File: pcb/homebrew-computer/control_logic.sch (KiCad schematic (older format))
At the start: 14 parts

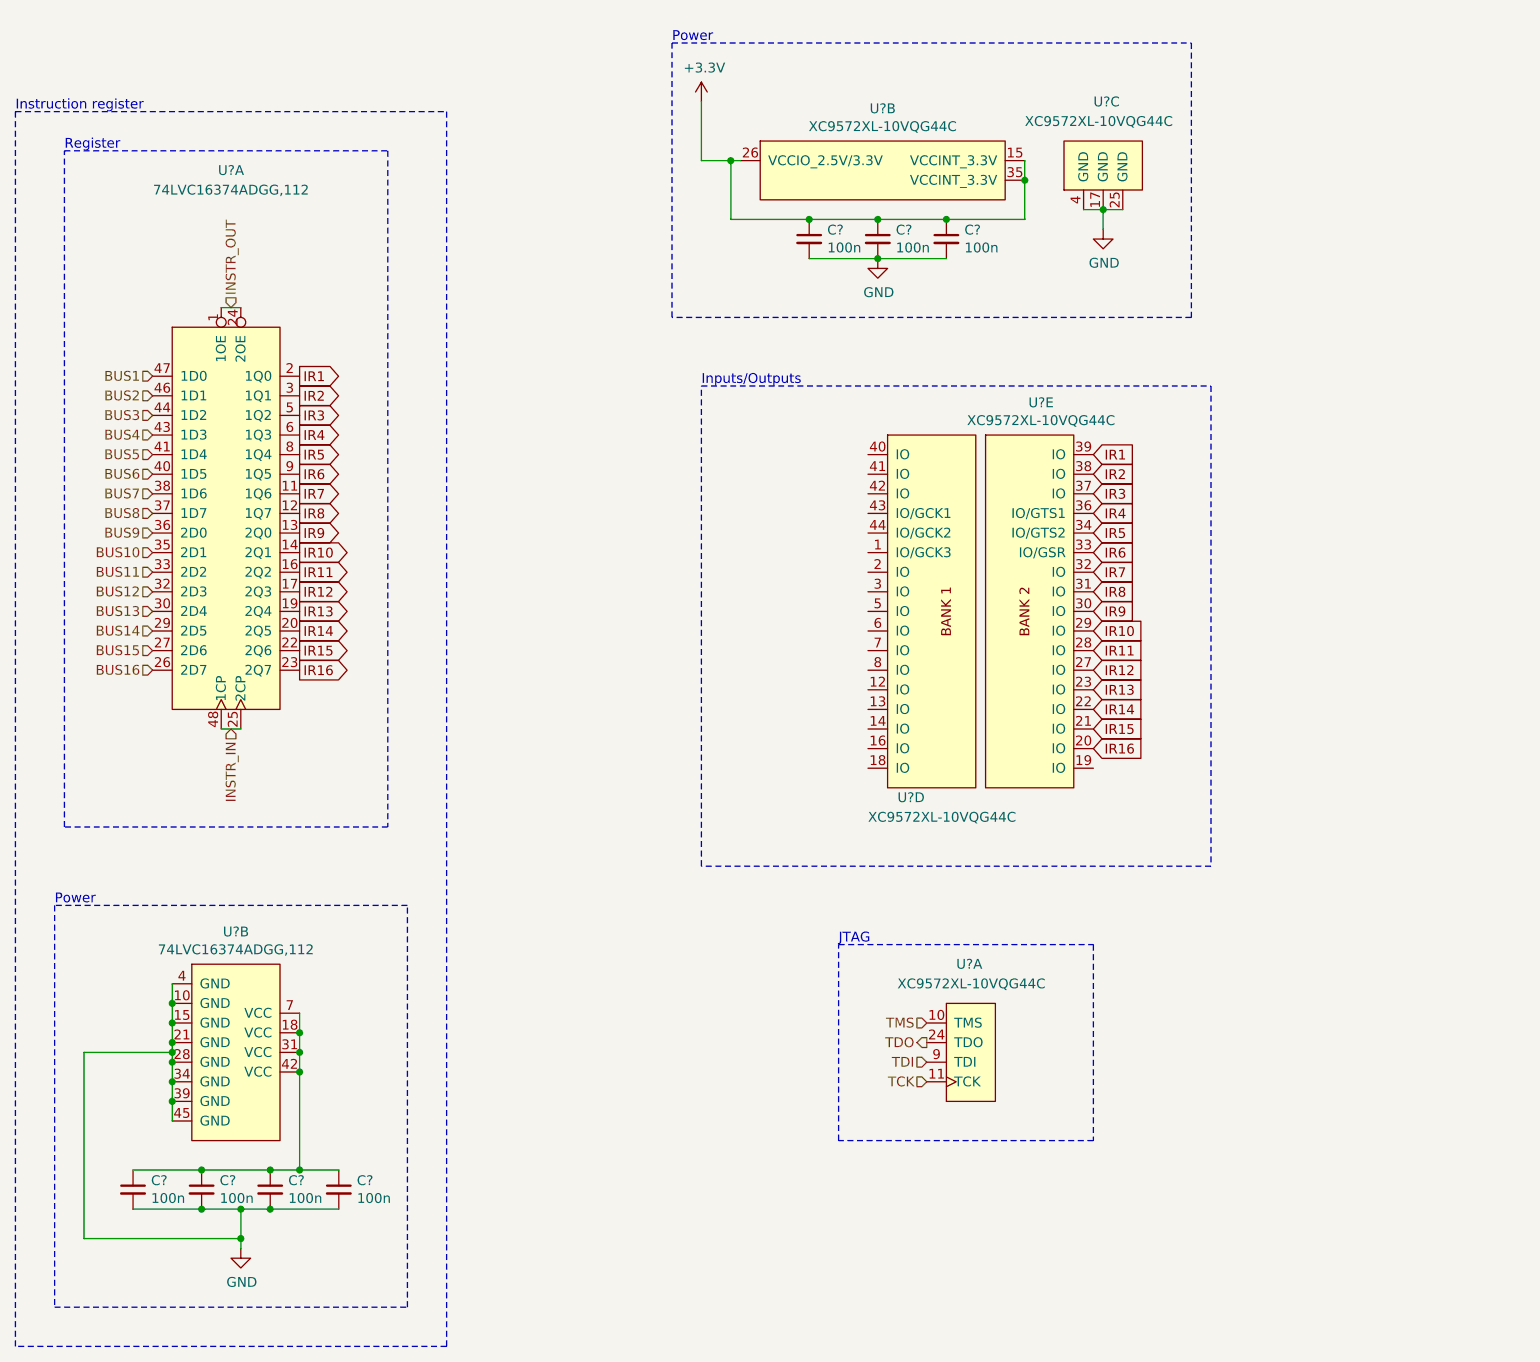
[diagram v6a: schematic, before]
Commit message: Change the control logic CPLD for a bigger one
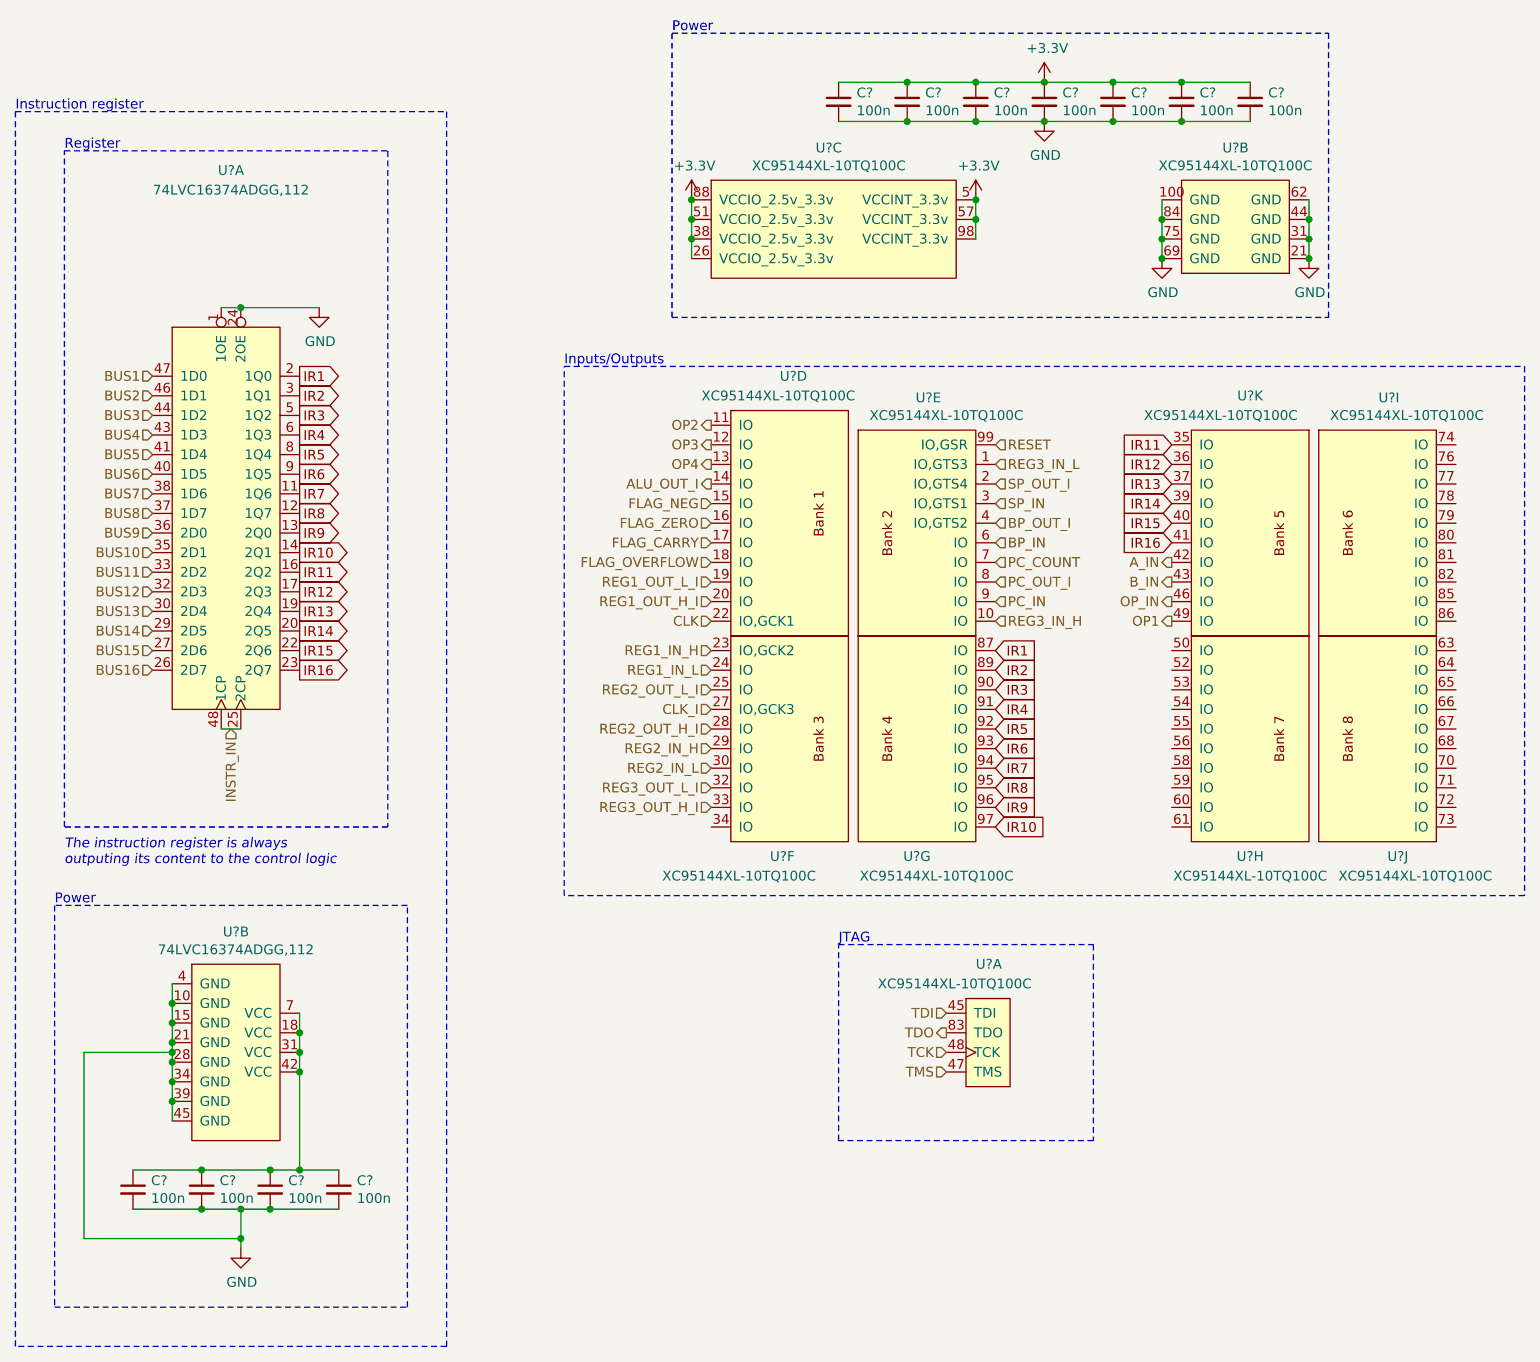
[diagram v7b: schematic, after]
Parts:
- removed U? (x5): XC9572XL-10VQG44C, symbol XC9500XL:XC9572XL-10VQG44C
- added C? (x4): 100n, symbol Device:C_Small
- added U? (x11): XC95144XL-10TQ100C, symbol XC9500XL:XC95144XL-10TQ100C
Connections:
- net INSTR_OUT is gone; now on net GND: U?.1 (1OE), U?.24 (2OE)
- net +3V3: now also C?.1, C?.1, C?.1, C?.1, U?.26 (VCCIO_2.5v_3.3v), U?.38 (VCCIO_2.5v_3.3v), U?.5 (VCCINT_3.3v), U?.51 (VCCIO_2.5v_3.3v), U?.57 (VCCINT_3.3v), U?.88 (VCCIO_2.5v_3.3v), U?.98 (VCCINT_3.3v)
- net GND: now also C?.2, C?.2, C?.2, C?.2, U?.100 (GND), U?.21 (GND), U?.31 (GND), U?.44 (GND), U?.62 (GND), U?.69 (GND), U?.75 (GND), U?.84 (GND)
- net IR1: now also U?.87 (IO)
- net IR10: now also U?.97 (IO)
- net IR11: now also U?.35 (IO)
- net IR12: now also U?.36 (IO)
- net IR13: now also U?.37 (IO)
- net IR14: now also U?.39 (IO)
- net IR15: now also U?.40 (IO)
- net IR16: now also U?.41 (IO)
- net IR2: now also U?.89 (IO)
- net IR3: now also U?.90 (IO)
- net IR4: now also U?.91 (IO)
- net IR5: now also U?.92 (IO)
- net IR6: now also U?.93 (IO)
- net IR7: now also U?.94 (IO)
- net IR8: now also U?.95 (IO)
- net IR9: now also U?.96 (IO)
- net TCK: now also U?.48 (TCK)
- net TDI: now also U?.45 (TDI)
- net TDO: now also U?.83 (TDO)
- net TMS: now also U?.47 (TMS)
- new net ALU_OUT_I: U?.14 (IO)
- new net A_IN: U?.42 (IO)
- new net BP_IN: U?.6 (IO)
- new net BP_OUT_I: U?.4 (IO,GTS2)
- new net B_IN: U?.43 (IO)
- new net CLK: U?.22 (IO,GCK1)
- new net CLK_I: U?.27 (IO,GCK3)
- new net FLAG_CARRY: U?.17 (IO)
- new net FLAG_NEG: U?.15 (IO)
- new net FLAG_OVERFLOW: U?.18 (IO)
- new net FLAG_ZERO: U?.16 (IO)
- new net OP1: U?.49 (IO)
- new net OP2: U?.11 (IO)
- new net OP3: U?.12 (IO)
- new net OP4: U?.13 (IO)
- new net OP_IN: U?.46 (IO)
- new net PC_COUNT: U?.7 (IO)
- new net PC_IN: U?.9 (IO)
- new net PC_OUT_I: U?.8 (IO)
- new net REG1_IN_H: U?.23 (IO,GCK2)
- new net REG1_IN_L: U?.24 (IO)
- new net REG1_OUT_H_I: U?.20 (IO)
- new net REG1_OUT_L_I: U?.19 (IO)
- new net REG2_IN_H: U?.29 (IO)
- new net REG2_IN_L: U?.30 (IO)
- new net REG2_OUT_H_I: U?.28 (IO)
- new net REG2_OUT_L_I: U?.25 (IO)
- new net REG3_IN_H: U?.10 (IO)
- new net REG3_IN_L: U?.1 (IO,GTS3)
- new net REG3_OUT_H_I: U?.33 (IO)
- new net REG3_OUT_L_I: U?.32 (IO)
- new net RESET: U?.99 (IO,GSR)
- new net SP_IN: U?.3 (IO,GTS1)
- new net SP_OUT_I: U?.2 (IO,GTS4)
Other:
- note added: "The instruction register is always\noutputing its content to the control logic"
- moved on the sheet: C?
